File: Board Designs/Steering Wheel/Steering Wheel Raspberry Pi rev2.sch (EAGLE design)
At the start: 7 parts, among them X1 CONNECTOR-4

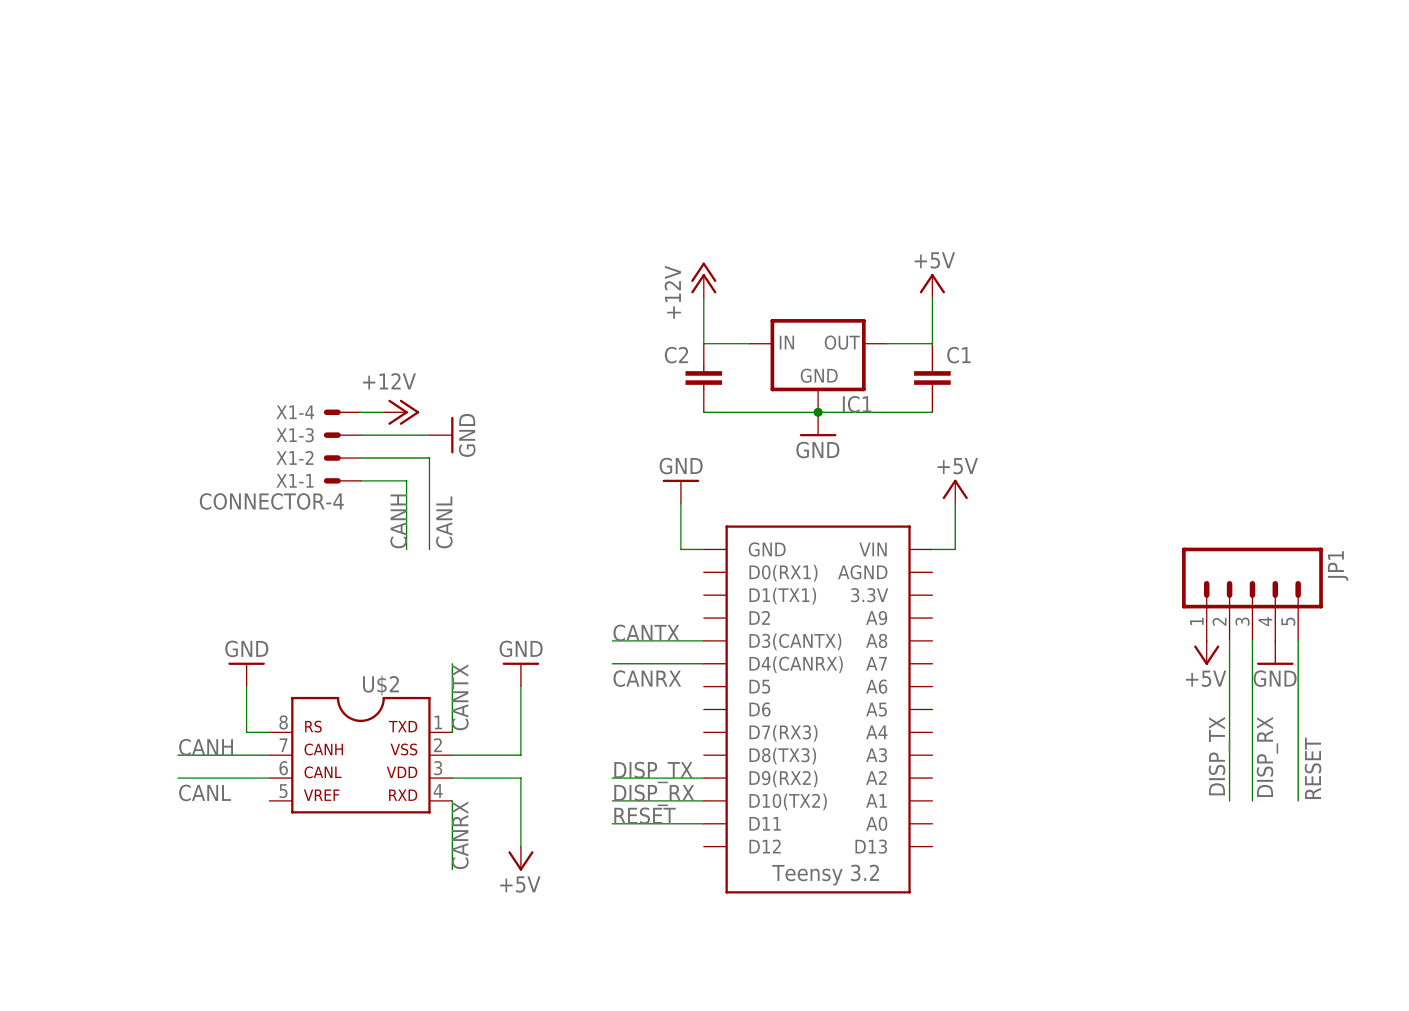
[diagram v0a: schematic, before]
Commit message: Created adapter board for teensy to interface w/ steering wheel display
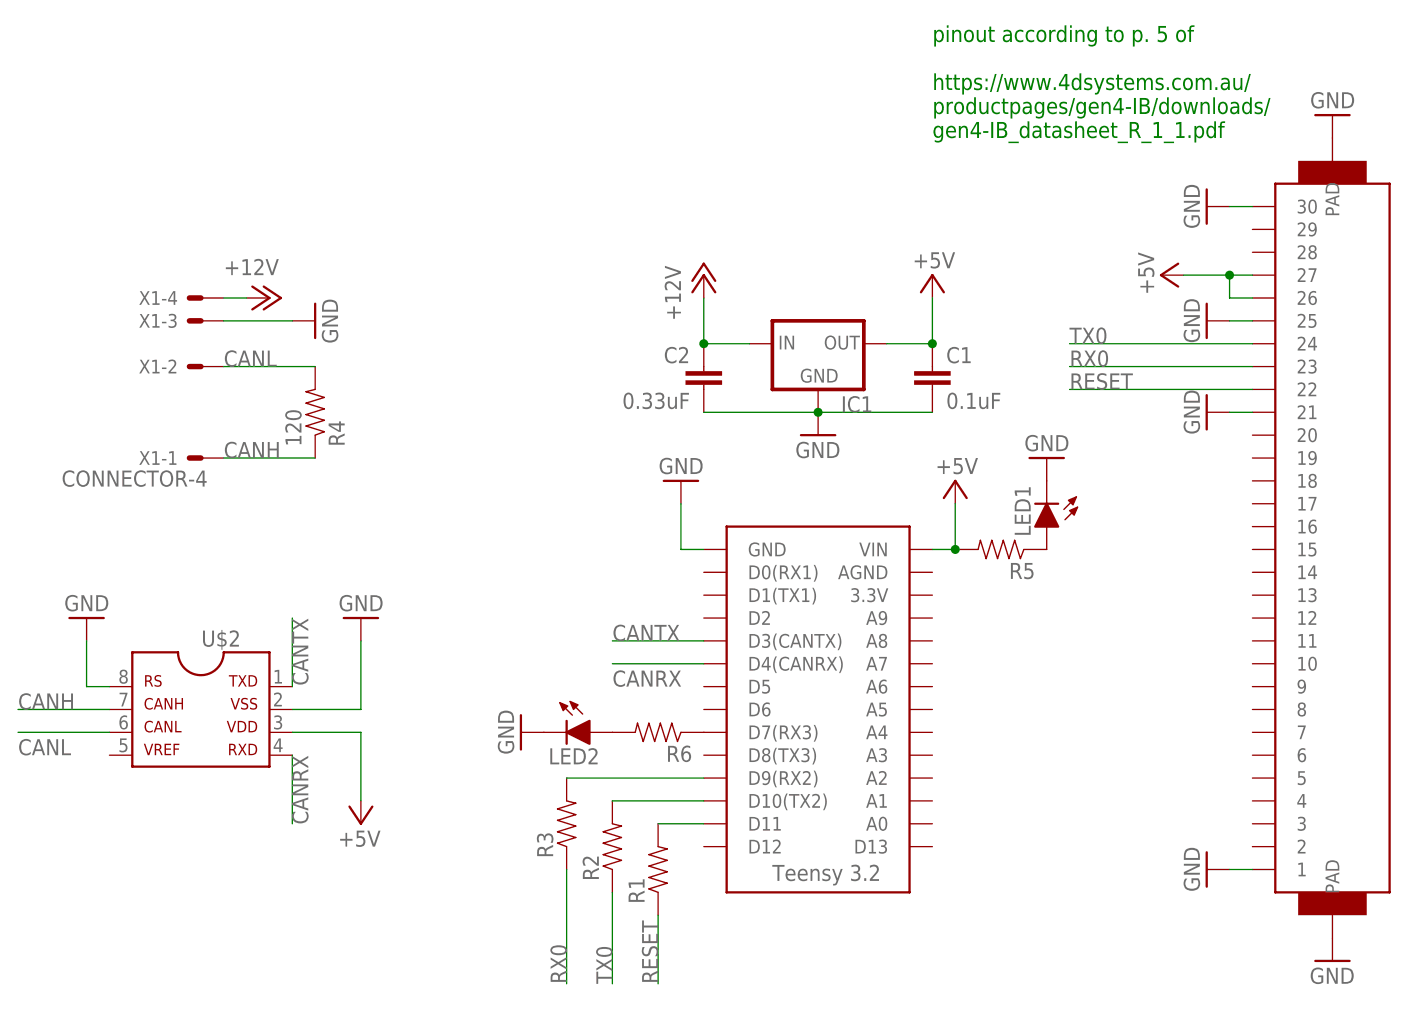
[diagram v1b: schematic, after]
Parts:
- removed JP1: (no value), HyTechDevices:M05
- added LED1, LED2: (no value), HyTechDevices:LED-0805
- added R1, R2, R3, R5, R6: (no value), HyTechDevices:RESISTOR0805-RES
- added R4: 120, HyTechDevices:RESISTOR0805-RES
- added U$3: FFC-30P-0.5MM, HyTechDevices:FFC-30P-0.5MM
- C1: value (none) -> 0.1uF
- C2: value (none) -> 0.33uF
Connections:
- removed net DISP_RX: JP1.3, U$1.D10(TX2)
- removed net DISP_TX: JP1.2, U$1.D9(RX2)
- new net N$1: LED1.A, R5.1
- new net N$2: R6.1, U$1.D7(RX3)
- new net N$3: LED2.A, R6.2
- new net RX0: R3.1, U$3.23
- new net TX0: R2.1, U$3.24
- new net UC_RST: R1.2, U$1.D11
- new net UC_RX: R3.2, U$1.D9(RX2)
- new net UC_TX: R2.2, U$1.D10(TX2)
- net +5V: now also R5.2, U$3.26, U$3.27; no longer JP1.1
- net CANH: now also R4.1
- net CANL: now also R4.2
- net GND: now also LED1.C, LED2.C, U$3.1, U$3.21, U$3.25, U$3.30, U$3.PAD@0, U$3.PAD@1; no longer JP1.4
- net RESET: now also R1.1, U$3.22; no longer JP1.5, U$1.D11
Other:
- note added: "pinout according to p. 5 of https://www.4dsystems.com.au/ productpages/gen4-IB/downloads/ gen4-IB_datasheet_R_1_1.pdf"
- moved on the sheet: U$2, X1-1, X1-2, X1-3, X1-4
